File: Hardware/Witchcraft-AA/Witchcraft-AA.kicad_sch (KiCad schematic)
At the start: 0 parts

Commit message: Some chances to start/rectangle-buttons in mech, and startedmaking the M.2 ports.
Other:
- note added: "Specs: -------- 4x USB-C 2x M.2 1x PCIe x4 card-slot 1x SDcard -------- Battery: -------- Samsung Galaxy S22 ultra's 5000 mAh, 3.86V"
- note removed: "Specs: -------- 4x USB-C 2x M.2 1x PCIe x8 card-slot 1x SDcard -------- Battery: -------- Samsung Galaxy S22 ultra's 5000 mAh, 3.86V"
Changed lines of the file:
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@@
     (rev "A-A")
   )
-  (text "Specs:\n--------\n\n4x USB-C\n\n2x M.2\n\n1x PCIe x8 card-slot\n\n1x SDcard\n\n\n--------\nBattery:\n--------\nSamsung Galaxy S22 ultra's 5000 mAh, 3.86V\n"
+  (text "Specs:\n--------\n\n4x USB-C\n\n2x M.2\n\n1x PCIe x4 card-slot\n\n1x SDcard\n\n\n--------\nBattery:\n--------\nSamsung Galaxy S22 ultra's 5000 mAh, 3.86V\n"
     (at 25.4 101.6 0)
     (effects (font (size 1.27 1.27)) (justify left bottom))
   )
   (text "Battery-cell manufacturers:\n--------------------------\nPanasonic/Sanyo \nSamsung \nLG \nSony\nSK Innovation"
-    (at 27.94 176.53 0)
+    (at 22.86 177.8 0)
     (effects (font (size 1.524 1.524)) (justify left bottom))
   )

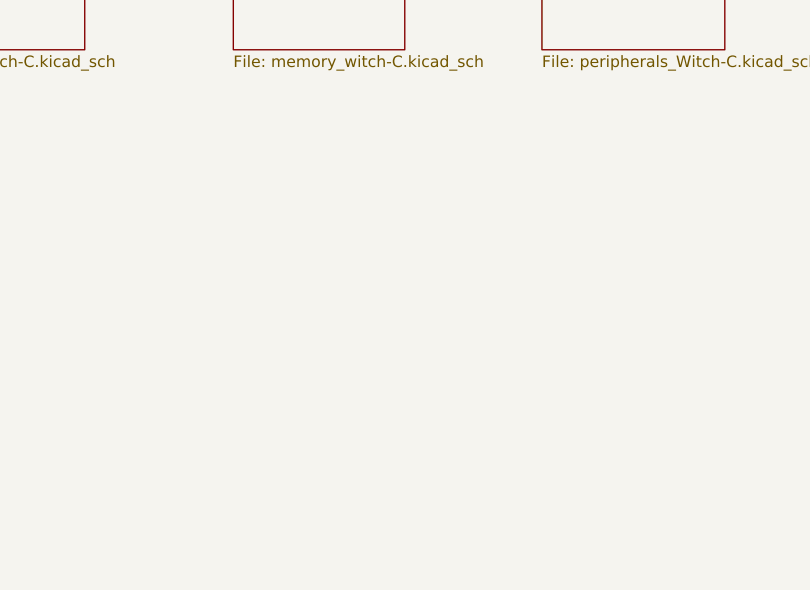
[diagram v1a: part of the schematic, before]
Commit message: added some reference-pictures for tracking down a suitable cooling-solution.
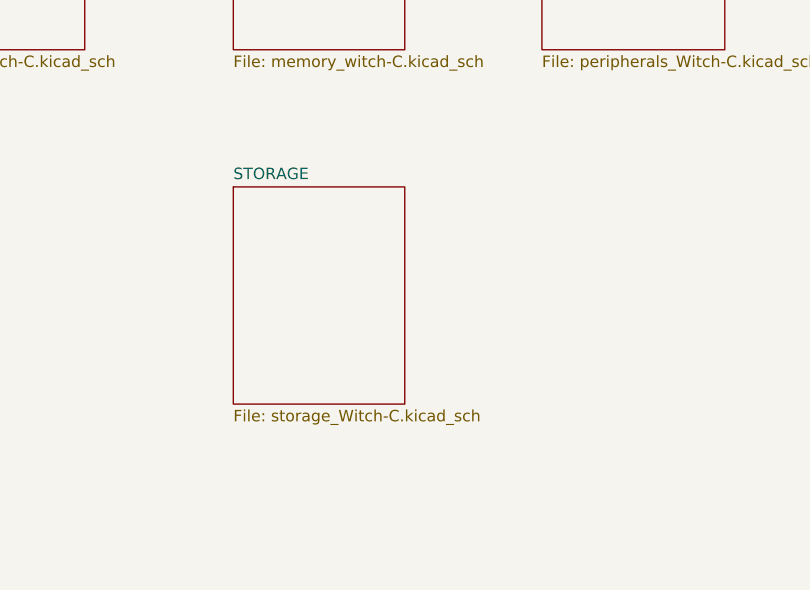
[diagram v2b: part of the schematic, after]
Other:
- added sheet STORAGE (storage_Witch-C.kicad_sch)
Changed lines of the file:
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@@
     (effects (font (size 1.524 1.524)) (justify left bottom))
+  )
+  (sheet (at 209.55 74.93) (size 19.05 24.13) (fields_autoplaced)
+    (stroke (width 0.1524) (type solid))
+    (fill (color 0 0 0 0.0000))
+    (property "Sheetname" "STORAGE" (at 209.55 74.2184 0)
+      (effects (font (size 1.27 1.27)) (justify left bottom))
+    )
+    (property "Sheetfile" "storage_Witch-C.kicad_sch" (at 209.55 99.6446 0)
+      (effects (font (size 1.27 1.27)) (justify left top))
+    )
+    (instances
+      (project "Witchcraft-AA"
+        (path "/0a9e17f7-244d-438d-bc29-a2e2d0831441" (page "7"))
+      )
+    )
   )
   (sheet (at 243.84 35.56) (size 20.32 24.13) (fields_autoplaced)

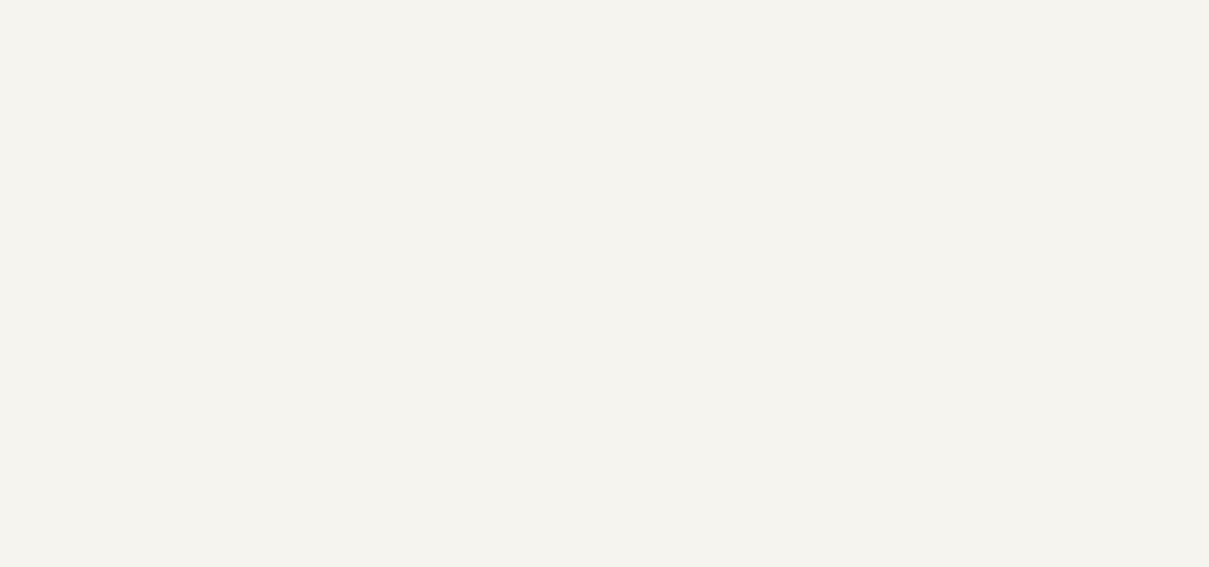
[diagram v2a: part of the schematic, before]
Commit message: Scrapped the custom-cooler design entirely, and went for a Blower-fan design instead. Got the fan-model mostly ready, now begins work on the fin-stack.
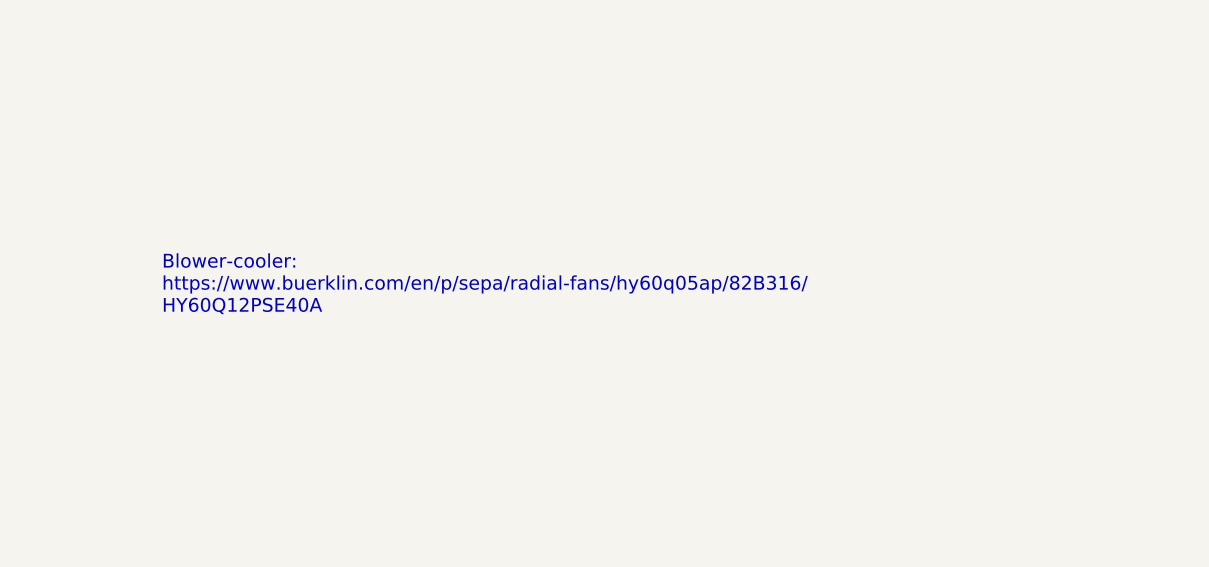
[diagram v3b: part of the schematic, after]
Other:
- note added: "Blower-cooler: https://www.buerklin.com/en/p/sepa/radial-fans/hy60q05ap/82B316/ HY60Q12PSE40A"
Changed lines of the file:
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@@
+    (effects (font (size 1.524 1.524)) (justify left bottom))
+  )
+  (text "Blower-cooler:\nhttps://www.buerklin.com/en/p/sepa/radial-fans/hy60q05ap/82B316/\nHY60Q12PSE40A"
+    (at 89.535 137.16 0)
     (effects (font (size 1.524 1.524)) (justify left bottom))
   )

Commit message: Almost completed the design of the new finstack, and have begun work on a redesign of cold-plate and rearrangement of components
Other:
- note added: "Blower-cooler: https://www.buerklin.com/en/p/sepa/radial-fans/hy60q05ap/82B316/ HY60Q12PSE40A https://detail.1688.com/offer/583163788768.html&scm=1007.45324.348050.0&pvid=69bee12b-f085-4bc8-93a7-4adfe971f483?spm=a262cb.19918180.ljxo5qvc.2.1fdf3a6eostrMb&file=583163788768.html&scm=1007.45324.348050.0&pvid=69bee12b-f085-4bc8-93a7-4adfe971f483"
- note removed: "Blower-cooler: https://www.buerklin.com/en/p/sepa/radial-fans/hy60q05ap/82B316/ HY60Q12PSE40A"
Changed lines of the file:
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@@
     (effects (font (size 1.524 1.524)) (justify left bottom))
   )
-  (text "Blower-cooler:\nhttps://www.buerklin.com/en/p/sepa/radial-fans/hy60q05ap/82B316/\nHY60Q12PSE40A"
-    (at 89.535 137.16 0)
+  (text "Blower-cooler:\nhttps://www.buerklin.com/en/p/sepa/radial-fans/hy60q05ap/82B316/\nHY60Q12PSE40A\n\nhttps://detail.1688.com/offer/583163788768.html&scm=1007.45324.348050.0&pvid=69bee12b-f085-4bc8-93a7-4adfe971f483?spm=a262cb.19918180.ljxo5qvc.2.1fdf3a6eostrMb&file=583163788768.html&scm=1007.45324.348050.0&pvid=69bee12b-f085-4bc8-93a7-4adfe971f483"
+    (at 65.405 140.97 0)
     (effects (font (size 1.524 1.524)) (justify left bottom))
   )
@@
     (fill (color 0 0 0 0.0000))
     (property "Sheetname" "STORAGE" (at 209.55 74.2184 0)
-      (effects (font (size 1.27 1.27)) (justify left bottom))
+      (effects (font (size 1.27 1.27) bold) (justify left bottom))
     )
     (property "Sheetfile" "storage_Witch-C.kicad_sch" (at 209.55 99.6446 0)

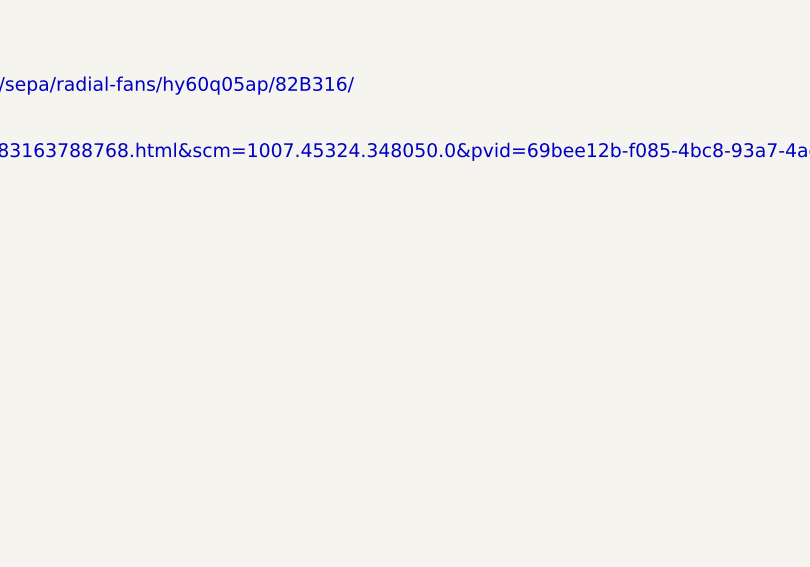
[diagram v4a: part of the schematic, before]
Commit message: ECAD: replaced the Z1 Extreme with the 7840U chip, as the AI-engine will be more useful for makers and non-gamers. MCAD: continued converting the outer shell towards a Assembly4-architecture, adding more items. Started a big change in design wherein I'm splitting the shell-design into a modular one, to accomodate removable controllers. Made some minor tweaks to the cooling-assembly, to accomodate the new, split shell-design. Updated the Readme to describe the project.
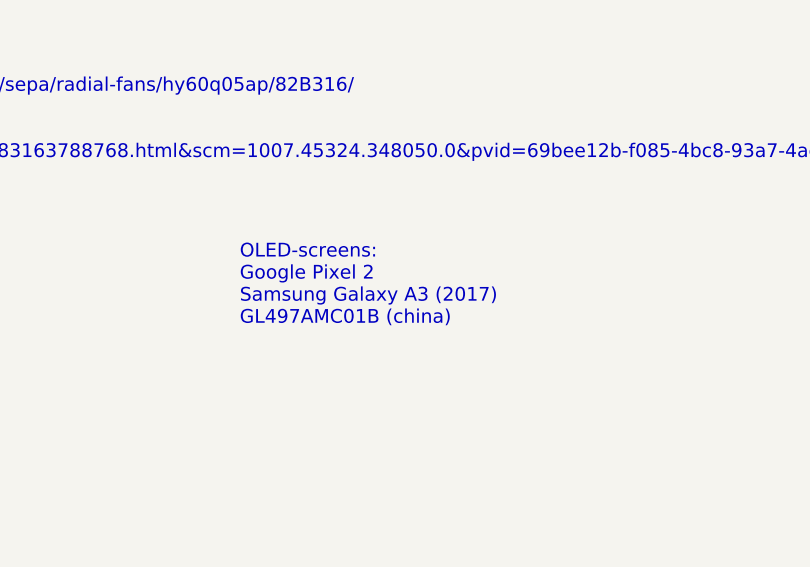
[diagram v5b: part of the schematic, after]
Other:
- note added: "OLED-screens: Google Pixel 2 Samsung Galaxy A3 (2017) GL497AMC01B (china)"
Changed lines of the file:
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@@
     (effects (font (size 1.27 1.27)) (justify left bottom))
+  )
+  (text "OLED-screens:\nGoogle Pixel 2\nSamsung Galaxy A3 (2017)\nGL497AMC01B (china)\n"
+    (at 124.46 159.385 0)
+    (effects (font (size 1.524 1.524)) (justify left bottom))
   )
   (text "Battery-cell manufacturers:\n--------------------------\nPanasonic/Sanyo \nSamsung \nLG \nSony\nSK Innovation"

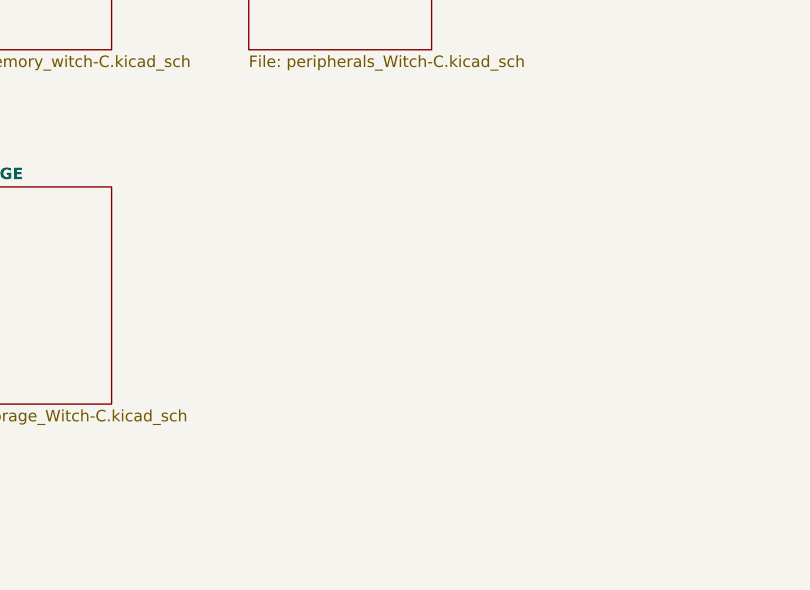
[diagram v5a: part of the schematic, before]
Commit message: MCAD: Added Oculink connector. ECAD: Added Oculink connector.
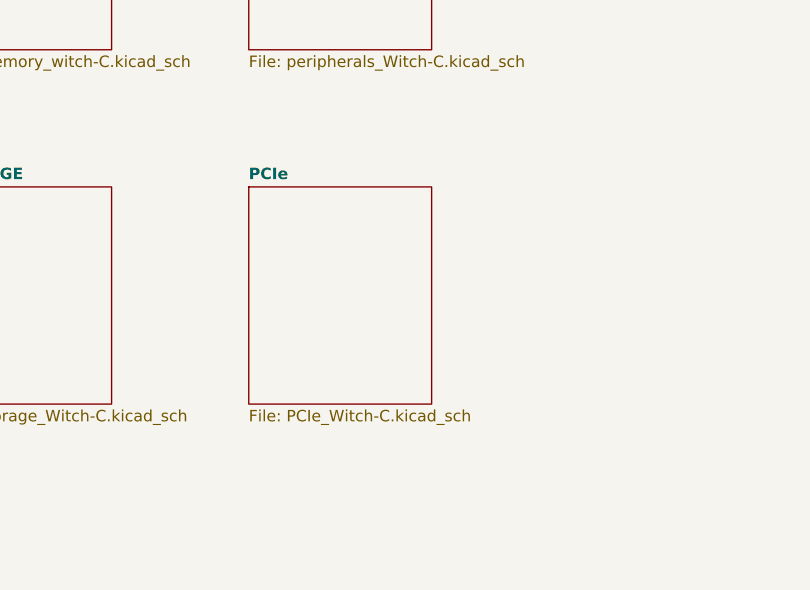
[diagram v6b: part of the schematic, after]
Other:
- added sheet PCIe (PCIe_Witch-C.kicad_sch)
- title: (none) -> WITCHCRAFT HANDHELD
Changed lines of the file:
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@@
   (paper "A3")
   (title_block
+    (title "WITCHCRAFT HANDHELD")
     (date "2023-05-06")
     (rev "A-A")
@@
       )
     )
+  )
+  (sheet (at 243.84 74.93) (size 20.32 24.13) (fields_autoplaced)
+    (stroke (width 0.1524) (type solid))
+    (fill (color 0 0 0 0.0000))
+    (property "Sheetname" "PCIe" (at 243.84 74.2184 0)
+      (effects (font (size 1.27 1.27) bold) (justify left bottom))
+    )
+    (property "Sheetfile" "PCIe_Witch-C.kicad_sch" (at 243.84 99.6446 0)
+      (effects (font (size 1.27 1.27)) (justify left top))
+    )
+    (instances
+      (project "Witchcraft-AA"
+        (path "/0a9e17f7-244d-438d-bc29-a2e2d0831441" (page "8"))
+      )
+    )
